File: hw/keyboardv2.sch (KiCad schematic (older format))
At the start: 22 parts, among them P3 CONN_4, Q1 MOSFET_N, SW1 SW_PUSH, U1 TINYMEGA, U2 74HC595

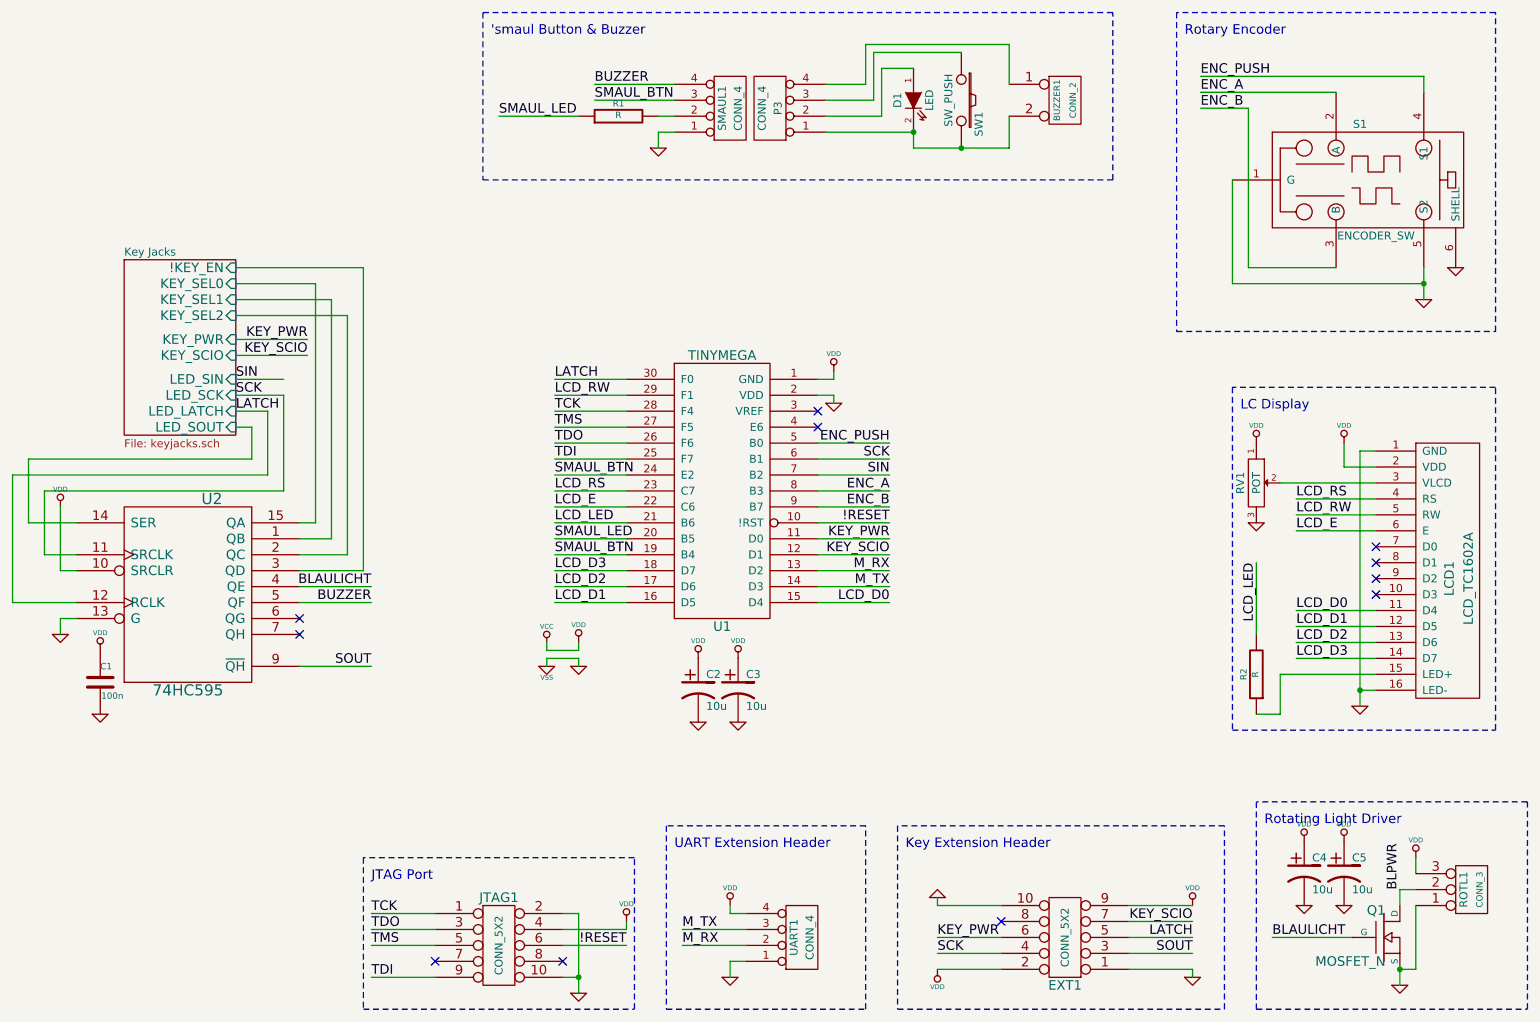
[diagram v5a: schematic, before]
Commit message: Assign LED resistor values, change some labels for readability
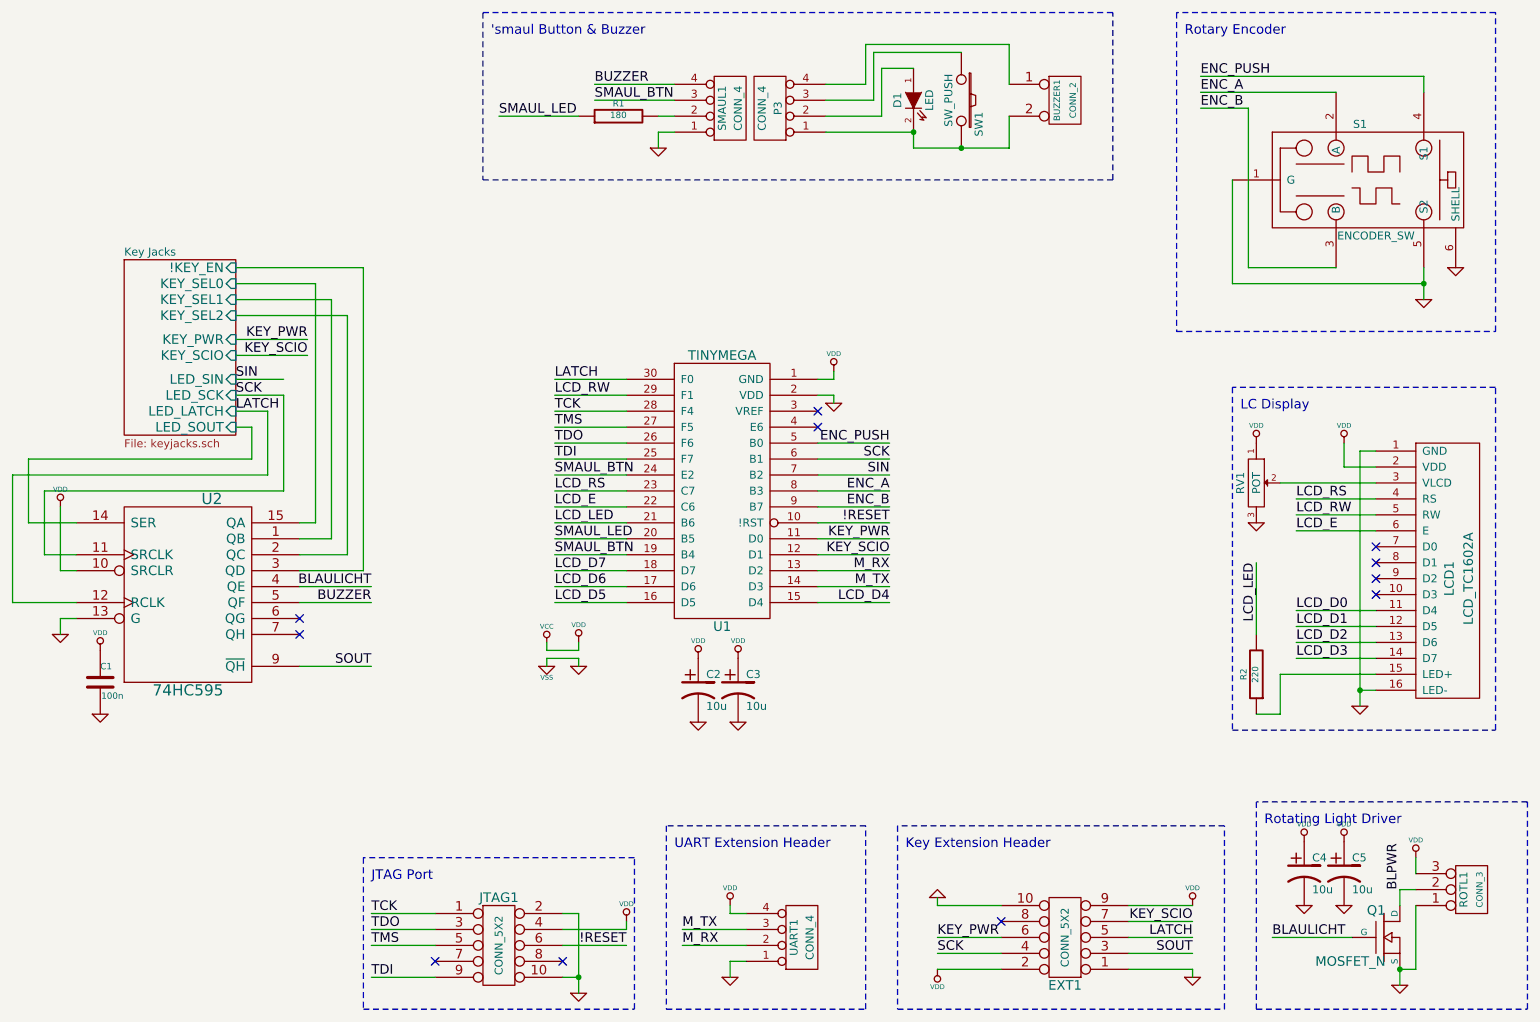
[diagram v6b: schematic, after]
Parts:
- R1: value R -> 180
- R2: value R -> 220
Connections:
- net LCD_D0: no longer U1.15 (D4)
- net LCD_D1: no longer U1.16 (D5)
- net LCD_D2: no longer U1.17 (D6)
- net LCD_D3: no longer U1.18 (D7)
- new net LCD_D4: U1.15 (D4)
- new net LCD_D5: U1.16 (D5)
- new net LCD_D6: U1.17 (D6)
- new net LCD_D7: U1.18 (D7)
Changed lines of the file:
@@
 Sheet 1 2
 Title ""
-Date "17 nov 2013"
+Date "1 dec 2013"
 Rev ""
 Comp ""
@@
 P 5400 1400
 F 0 "R1" V 5480 1400 40  0000 C CNN
-F 1 "R" V 5407 1401 40  0000 C CNN
+F 1 "180" V 5407 1401 40  0000 C CNN
 F 2 "~" V 5330 1400 30  0000 C CNN
 F 3 "~" H 5400 1400 30  0000 C CNN
@@
 	5000 4250 5450 4250
 Text Label 7100 4450 2    60   ~ 0
-LCD_D0
+LCD_D4
 Text Label 5000 4450 0    60   ~ 0
-LCD_D1
+LCD_D5
 Text Label 5000 4350 0    60   ~ 0
-LCD_D2
+LCD_D6
 Text Label 5000 4250 0    60   ~ 0
-LCD_D3
+LCD_D7
 Wire Wire Line
 	5450 4050 5000 4050
@@
 P 9400 4900
 F 0 "R2" V 9480 4900 40  0000 C CNN
-F 1 "R" V 9407 4901 40  0000 C CNN
+F 1 "220" V 9407 4901 40  0000 C CNN
 F 2 "~" V 9330 4900 30  0000 C CNN
 F 3 "~" H 9400 4900 30  0000 C CNN
